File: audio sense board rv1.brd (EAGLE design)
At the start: 94.9 x 35.6 mm, 36 parts, among them IC1 A000053, IC2 TSOP38238, J1 PJRAN1X1U01X, J4 PJRAN1X1U01X, Q1 2N3904, Q2 2N3904

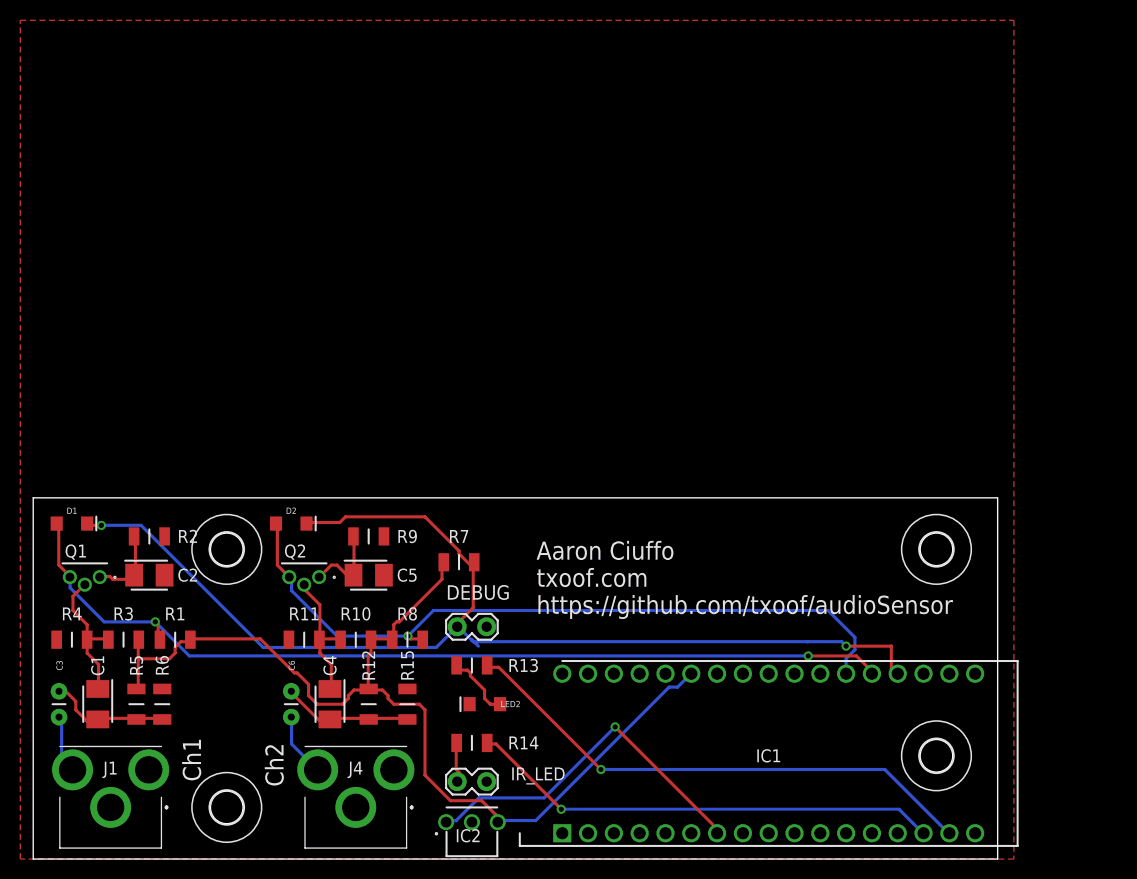
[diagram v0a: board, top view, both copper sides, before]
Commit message: add ground pour on bottom
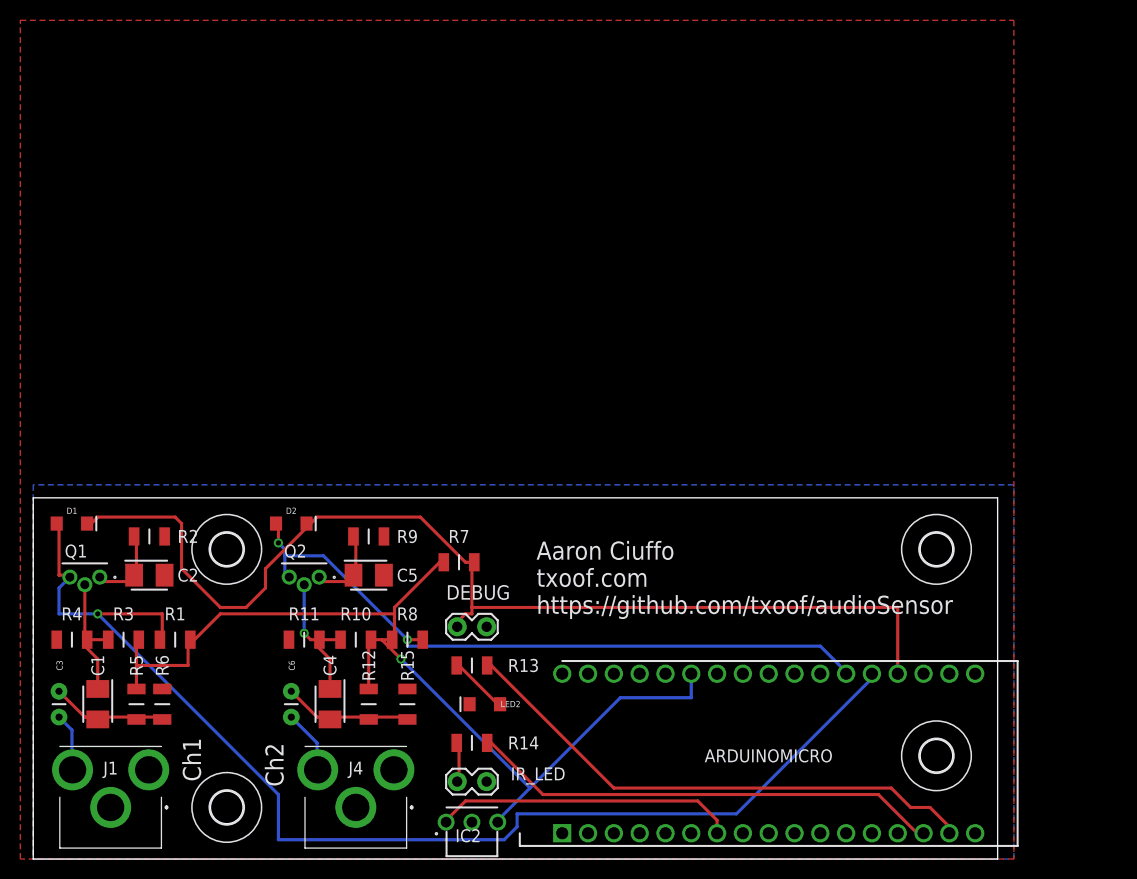
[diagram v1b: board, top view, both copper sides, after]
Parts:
- renumbered IC1 to ARDUINOMICRO
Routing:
- net N$2: track 92.2 -> 119.2 mm, vias 2 -> 1
- net N$5: track 117.4 -> 108.1 mm, vias 2 -> 0
- net N$15: track 35.2 -> 29.7 mm, vias 1 -> 0
- net N$12: track 72.9 -> 68.1 mm, vias 1 -> 2
- net VCC: track 97.5 -> 98.6 mm, vias 0 -> 1
- net N$3: track 13.9 -> 13.1 mm
- net N$13: track 6.66 -> 5.85 mm
- net N$1: track 7.63 -> 8.33 mm
- net N$14: track 13.6 -> 14.0 mm, vias 0 -> 1
- net N$4: track 52.4 -> 52.7 mm, vias 1 -> 0
- net N$11: track 46.7 -> 46.6 mm, vias 1 -> 0
- added copper zone on layer 16, net GND

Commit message: rework led and signals
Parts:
- removed DEBUG: Debug Jumper, SparkFun-Connectors:1X02_LOCK
- removed R7: 10K, Samac Populated:RESC3216X60N
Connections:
- removed net N$12: ARDUINOMICRO.23, D2.A, Q2.3, R8.1
- removed net N$2: ARDUINOMICRO.22, D1.A, Q1.3, R1.1
- new net J1SIGNAL: ARDUINOMICRO.22, D1.A, R1.1
- new net J4SIGNAL: ARDUINOMICRO.23, D2.A, R8.1
- new net N$8: D1.C, Q1.3
- net GND: no longer DEBUG.2
- net N$5: now also Q2.3; no longer ARDUINOMICRO.21, D1.C, DEBUG.1, R7.1
- net VCC: no longer R7.2
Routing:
- net N$2: track 119.2 -> 0.00 mm, vias 1 -> 0
- net J1SIGNAL: track 0.00 -> 111.9 mm, vias 0 -> 1
- net N$5: track 108.1 -> 0.00 mm
- net N$12: track 68.1 -> 0.00 mm, vias 2 -> 0
- net VCC: track 98.6 -> 64.6 mm
